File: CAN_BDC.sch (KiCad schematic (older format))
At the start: 28 parts, among them P1 CONN_01X02, P2 CONN_01X05, P3 CONN_01X02, P4 CONN_01X02, P5 CONN_01X02, P6 CONN_01X02, P7 CONN_01X04, U1 PSD2CAN, U2 SN65HVD232D, U3 POLOLU_A4988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

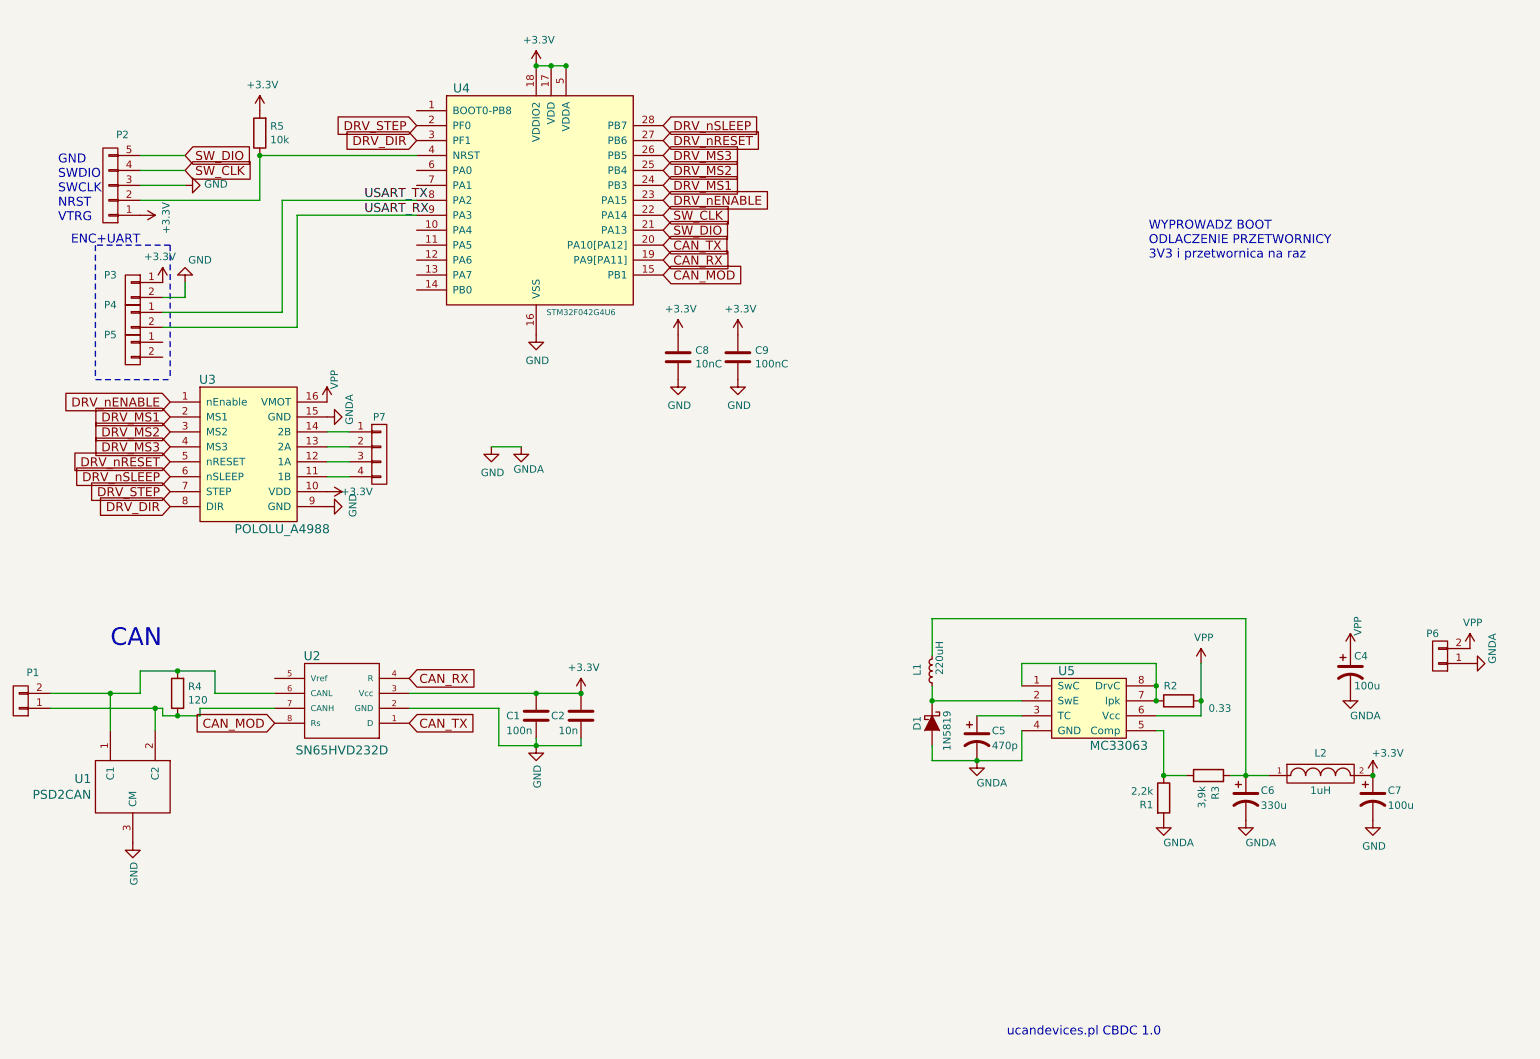
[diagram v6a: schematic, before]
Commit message: Bootconnector addition
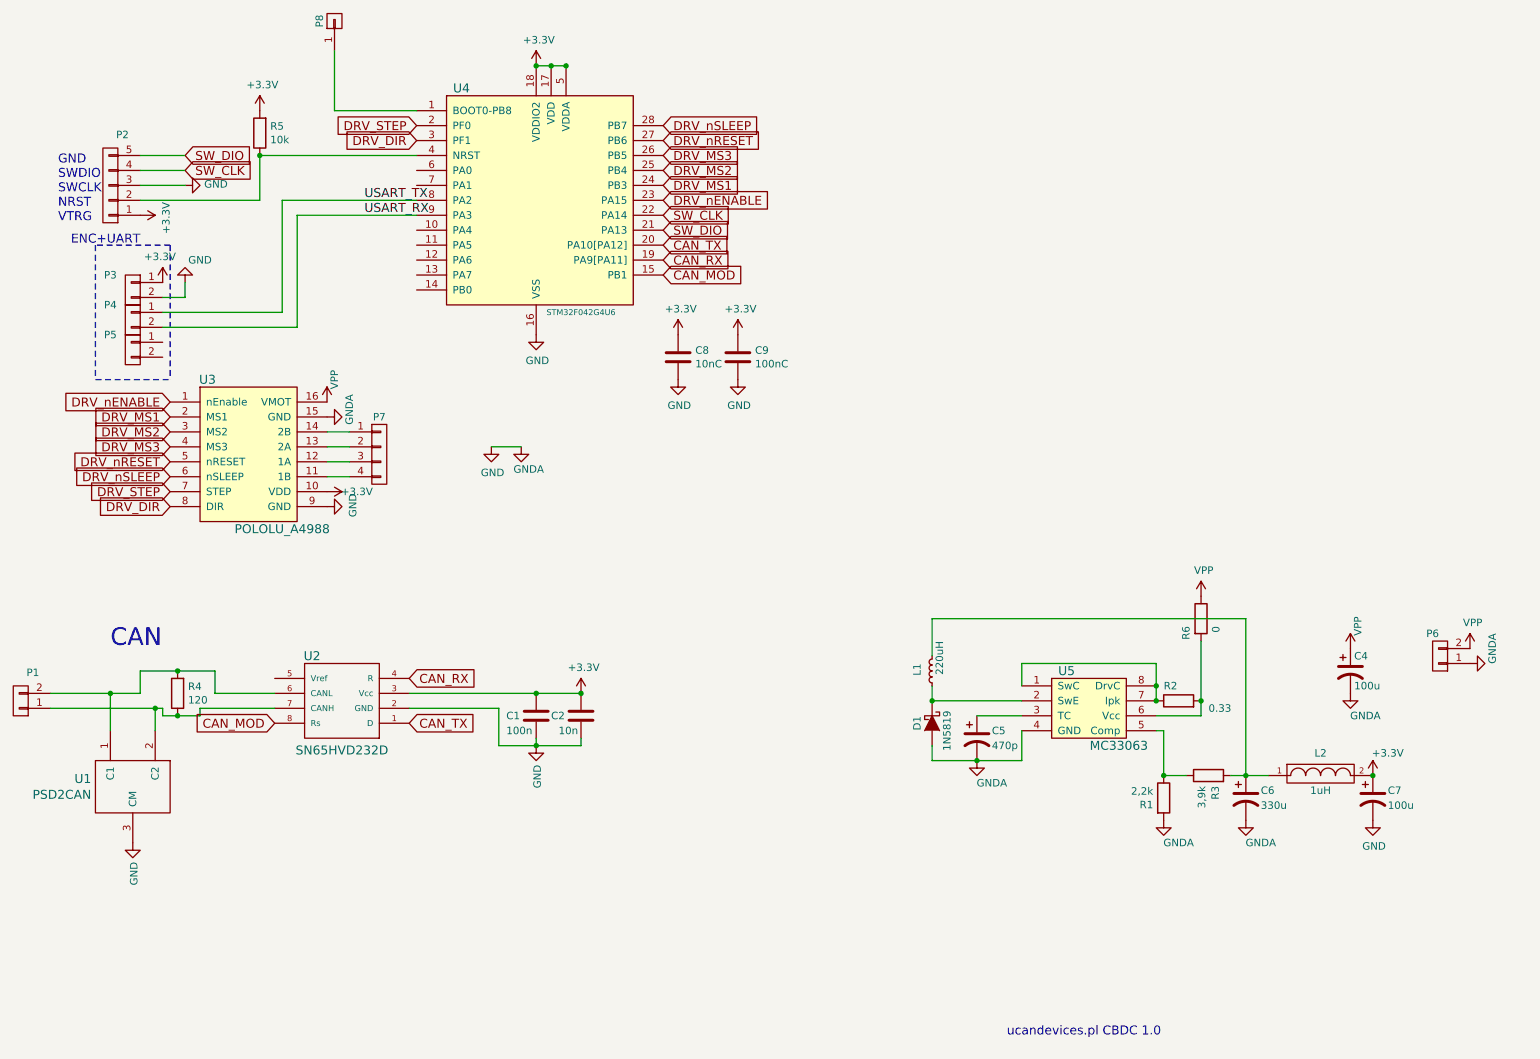
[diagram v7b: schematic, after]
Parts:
- added P8: CONN_01X01, usb_ccb_custom:smd1Conn, symbol CONN_01X01
- added R6: 0, Resistors_SMD:R_0603, symbol R
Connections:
- net VPP: now also R6.1; no longer R2.2, U5.6 (Vcc)
- net at U4.1 (BOOT0-PB8): now also P8.1 (P1)
- new net: R2.2, R6.2, U5.6 (Vcc)
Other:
- note removed: "WYPROWADZ BOOT\nODLACZENIE PRZETWORNICY\n3V3 i przetwornica na raz\n"
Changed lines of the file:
@@
 $EndDescr
 $Comp
-L GND #PWR01
+L GND #PWR14
 U 1 1 570561B2
 P 4250 2800
-F 0 "#PWR01" H 4250 2550 50  0001 C CNN
+F 0 "#PWR14" H 4250 2550 50  0001 C CNN
 F 1 "GND" H 4258 2627 50  0000 C CNN
 F 2 "" H 4250 2800 50  0000 C CNN
@@
 GND\nSWDIO\nSWCLK\nNRST\nVTRG
 $Comp
-L +3.3V #PWR02
+L +3.3V #PWR6
 U 1 1 5706E500
 P 2400 1300
-F 0 "#PWR02" H 2400 1150 50  0001 C CNN
+F 0 "#PWR6" H 2400 1150 50  0001 C CNN
 F 1 "+3.3V" H 2418 1473 50  0000 C CNN
 F 2 "" H 2400 1300 50  0000 C CNN
@@
 $EndComp
 $Comp
-L +3.3V #PWR03
+L +3.3V #PWR13
 U 1 1 5706E57B
 P 4250 1000
-F 0 "#PWR03" H 4250 850 50  0001 C CNN
+F 0 "#PWR13" H 4250 850 50  0001 C CNN
 F 1 "+3.3V" H 4268 1173 50  0000 C CNN
 F 2 "" H 4250 1000 50  0000 C CNN
@@
 $EndComp
 $Comp
-L GND #PWR04
+L GND #PWR18
 U 1 1 5706EDB2
 P 5200 3100
-F 0 "#PWR04" H 5200 2850 50  0001 C CNN
+F 0 "#PWR18" H 5200 2850 50  0001 C CNN
 F 1 "GND" H 5208 2927 50  0000 C CNN
 F 2 "" H 5200 3100 50  0000 C CNN
@@
 $EndComp
 $Comp
-L GND #PWR05
+L GND #PWR20
 U 1 1 5706EDDA
 P 5600 3100
-F 0 "#PWR05" H 5600 2850 50  0001 C CNN
+F 0 "#PWR20" H 5600 2850 50  0001 C CNN
 F 1 "GND" H 5608 2927 50  0000 C CNN
 F 2 "" H 5600 3100 50  0000 C CNN
@@
 $EndComp
 $Comp
-L +3.3V #PWR06
+L +3.3V #PWR19
 U 1 1 5706EE52
 P 5600 2800
-F 0 "#PWR06" H 5600 2650 50  0001 C CNN
+F 0 "#PWR19" H 5600 2650 50  0001 C CNN
 F 1 "+3.3V" H 5618 2973 50  0000 C CNN
 F 2 "" H 5600 2800 50  0000 C CNN
@@
 $EndComp
 $Comp
-L +3.3V #PWR07
+L +3.3V #PWR17
 U 1 1 5706EEDE
 P 5200 2800
-F 0 "#PWR07" H 5200 2650 50  0001 C CNN
+F 0 "#PWR17" H 5200 2650 50  0001 C CNN
 F 1 "+3.3V" H 5218 2973 50  0000 C CNN
 F 2 "" H 5200 2800 50  0000 C CNN
@@
 $EndComp
 $Comp
-L +3.3V #PWR08
+L +3.3V #PWR16
 U 1 1 5708A6C5
 P 4550 5200
-F 0 "#PWR08" H 4550 5050 50  0001 C CNN
+F 0 "#PWR16" H 4550 5050 50  0001 C CNN
 F 1 "+3.3V" H 4568 5373 50  0000 C CNN
 F 2 "" H 4550 5200 50  0000 C CNN
@@
 $EndComp
 $Comp
-L GND #PWR09
+L GND #PWR15
 U 1 1 5708A9FB
 P 4250 5550
-F 0 "#PWR09" H 4250 5300 50  0001 C CNN
+F 0 "#PWR15" H 4250 5300 50  0001 C CNN
 F 1 "GND" V 4258 5422 50  0000 R CNN
 F 2 "" H 4250 5550 50  0000 C CNN
@@
 $EndComp
 $Comp
-L GND #PWR010
+L GND #PWR1
 U 1 1 5708D67B
 P 1550 6200
-F 0 "#PWR010" H 1550 5950 50  0001 C CNN
+F 0 "#PWR1" H 1550 5950 50  0001 C CNN
 F 1 "GND" V 1558 6072 50  0000 R CNN
 F 2 "" H 1550 6200 50  0000 C CNN
@@
 SW_DIO
 $Comp
-L GND #PWR011
+L GND #PWR5
 U 1 1 571ACD79
 P 1900 2450
-F 0 "#PWR011" H 1900 2200 50  0001 C CNN
+F 0 "#PWR5" H 1900 2200 50  0001 C CNN
 F 1 "GND" H 2000 2300 50  0000 C CNN
 F 2 "" H 1900 2450 50  0000 C CNN
@@
 $EndComp
 $Comp
-L +3.3V #PWR012
+L +3.3V #PWR2
 U 1 1 57800AA2
 P 1600 2000
-F 0 "#PWR012" H 1600 1850 50  0001 C CNN
+F 0 "#PWR2" H 1600 1850 50  0001 C CNN
 F 1 "+3.3V" H 1618 2173 50  0000 C CNN
 F 2 "" H 1600 2000 50  0000 C CNN
@@
 ucandevices.pl CBDC 1.0\n
 $Comp
-L +3.3V #PWR013
+L +3.3V #PWR3
 U 1 1 57F6DF04
 P 1750 2450
-F 0 "#PWR013" H 1750 2300 50  0001 C CNN
+F 0 "#PWR3" H 1750 2300 50  0001 C CNN
 F 1 "+3.3V" H 1768 2623 50  0000 C CNN
 F 2 "" H 1750 2450 50  0000 C CNN
@@
 $EndComp
 $Comp
-L +3.3V #PWR014
+L +3.3V #PWR27
 U 1 1 57F96BE3
 P 9850 5750
-F 0 "#PWR014" H 9850 5600 50  0001 C CNN
+F 0 "#PWR27" H 9850 5600 50  0001 C CNN
 F 1 "+3.3V" H 9950 5900 50  0000 C CNN
 F 2 "" H 9850 5750 50  0000 C CNN
@@
 $EndComp
 $Comp
-L GND #PWR015
+L GND #PWR4
 U 1 1 57056C83
 P 1900 1800
-F 0 "#PWR015" H 1900 1550 50  0001 C CNN
+F 0 "#PWR4" H 1900 1550 50  0001 C CNN
 F 1 "GND" V 1908 1672 50  0000 R CNN
 F 2 "" H 1900 1800 50  0000 C CNN
@@
 $EndComp
 $Comp
-L VPP #PWR016
+L VPP #PWR29
 U 1 1 5802A676
 P 10500 4900
-F 0 "#PWR016" H 10500 4750 50  0001 C CNN
+F 0 "#PWR29" H 10500 4750 50  0001 C CNN
 F 1 "VPP" H 10518 5073 50  0000 C CNN
 F 2 "" H 10500 4900 50  0000 C CNN
@@
 ENC+UART
 $Comp
-L GNDA #PWR017
+L GNDA #PWR30
 U 1 1 5805AC7E
 P 10500 5000
-F 0 "#PWR017" H 10500 4750 50  0001 C CNN
+F 0 "#PWR30" H 10500 4750 50  0001 C CNN
 F 1 "GNDA" H 10600 4850 50  0000 C CNN
 F 2 "" H 10500 5000 50  0000 C CNN
@@
 $EndComp
 $Comp
-L VPP #PWR018
+L VPP #PWR7
 U 1 1 5808D6A9
 P 2850 3250
-F 0 "#PWR018" H 2850 3100 50  0001 C CNN
+F 0 "#PWR7" H 2850 3100 50  0001 C CNN
 F 1 "VPP" V 2900 3400 50  0000 C CNN
 F 2 "" H 2850 3250 50  0000 C CNN
@@
 $EndComp
 $Comp
-L GNDA #PWR019
+L GNDA #PWR8
 U 1 1 5808DF8A
 P 2850 3350
-F 0 "#PWR019" H 2850 3100 50  0001 C CNN
+F 0 "#PWR8" H 2850 3100 50  0001 C CNN
 F 1 "GNDA" H 2900 3200 50  0000 C CNN
 F 2 "" H 2850 3350 50  0000 C CNN
@@
 DRV_MS3
 $Comp
-L +3.3V #PWR020
+L +3.3V #PWR9
 U 1 1 5809060D
 P 2850 3850
-F 0 "#PWR020" H 2850 3700 50  0001 C CNN
+F 0 "#PWR9" H 2850 3700 50  0001 C CNN
 F 1 "+3.3V" V 2850 4050 50  0000 C CNN
 F 2 "" H 2850 3850 50  0000 C CNN
@@
 $EndComp
 $Comp
-L GNDA #PWR021
+L GNDA #PWR26
 U 1 1 58095023
 P 9700 5200
-F 0 "#PWR021" H 9700 4950 50  0001 C CNN
+F 0 "#PWR26" H 9700 4950 50  0001 C CNN
 F 1 "GNDA" H 9800 5050 50  0000 C CNN
 F 2 "" H 9700 5200 50  0000 C CNN
@@
 $EndComp
 $Comp
-L VPP #PWR022
+L VPP #PWR25
 U 1 1 5809511F
 P 9700 4900
-F 0 "#PWR022" H 9700 4750 50  0001 C CNN
+F 0 "#PWR25" H 9700 4750 50  0001 C CNN
 F 1 "VPP" V 9750 5050 50  0000 C CNN
 F 2 "" H 9700 4900 50  0000 C CNN
@@
 Connection ~ 8400 5150
 $Comp
-L VPP #PWR023
+L VPP #PWR23
 U 1 1 580A2B8E
-P 8700 5000
-F 0 "#PWR023" H 8700 4850 50  0001 C CNN
-F 1 "VPP" H 8718 5173 50  0000 C CNN
-F 2 "" H 8700 5000 50  0000 C CNN
-F 3 "" H 8700 5000 50  0000 C CNN
-	1    8700 5000
-	1    0    0    -1
-$EndComp
-Wire Wire Line
-	8700 5000 8700 5350
+P 8700 4550
+F 0 "#PWR23" H 8700 4400 50  0001 C CNN
+F 1 "VPP" H 8718 4723 50  0000 C CNN
+F 2 "" H 8700 4550 50  0000 C CNN
+F 3 "" H 8700 4550 50  0000 C CNN
+	1    8700 4550
+	1    0    0    -1
+$EndComp
+Wire Wire Line
+	8700 4850 8700 5350
 Connection ~ 8700 5250
 Wire Wire Line
@@
 	8900 5750 9150 5750
 $Comp
-L GNDA #PWR024
+L GNDA #PWR21
 U 1 1 580A3786
 P 7200 5650
-F 0 "#PWR024" H 7200 5400 50  0001 C CNN
+F 0 "#PWR21" H 7200 5400 50  0001 C CNN
 F 1 "GNDA" H 7300 5500 50  0000 C CNN
 F 2 "" H 7200 5650 50  0000 C CNN
@@
 $EndComp
 $Comp
-L GNDA #PWR025
+L GNDA #PWR22
 U 1 1 580A3846
 P 8450 6050
-F 0 "#PWR025" H 8450 5800 50  0001 C CNN
+F 0 "#PWR22" H 8450 5800 50  0001 C CNN
 F 1 "GNDA" H 8550 5900 50  0000 C CNN
 F 2 "" H 8450 6050 50  0000 C CNN
@@
 $EndComp
 $Comp
-L GNDA #PWR026
+L GNDA #PWR24
 U 1 1 580A3906
 P 9000 6050
-F 0 "#PWR026" H 9000 5800 50  0001 C CNN
+F 0 "#PWR24" H 9000 5800 50  0001 C CNN
 F 1 "GNDA" H 9100 5900 50  0000 C CNN
 F 2 "" H 9000 6050 50  0000 C CNN
@@
 Connection ~ 9850 5750
 $Comp
-L GND #PWR027
+L GND #PWR28
 U 1 1 580A4A8C
 P 9850 6050
-F 0 "#PWR027" H 9850 5800 50  0001 C CNN
+F 0 "#PWR28" H 9850 5800 50  0001 C CNN
 F 1 "GND" H 9858 5877 50  0000 C CNN
 F 2 "" H 9850 6050 50  0000 C CNN
@@
 Connection ~ 8400 5250
 $Comp
-L GND #PWR028
+L GND #PWR10
 U 1 1 580A6796
 P 2850 3950
-F 0 "#PWR028" H 2850 3700 50  0001 C CNN
+F 0 "#PWR10" H 2850 3700 50  0001 C CNN
 F 1 "GND" H 2858 3777 50  0000 C CNN
 F 2 "" H 2850 3950 50  0000 C CNN
@@
 $EndComp
 $Comp
-L GNDA #PWR029
+L GNDA #PWR12
 U 1 1 580A6A98
 P 4150 3550
-F 0 "#PWR029" H 4150 3300 50  0001 C CNN
+F 0 "#PWR12" H 4150 3300 50  0001 C CNN
 F 1 "GNDA" H 4200 3400 50  0000 C CNN
 F 2 "" H 4150 3550 50  0000 C CNN
@@
 $EndComp
 $Comp
-L GND #PWR030
+L GND #PWR11
 U 1 1 580A6AF4
 P 3950 3550
-F 0 "#PWR030" H 3950 3300 50  0001 C CNN
+F 0 "#PWR11" H 3950 3300 50  0001 C CNN
 F 1 "GND" H 3958 3377 50  0000 C CNN
 F 2 "" H 3950 3550 50  0000 C CNN
@@
 	2100 5200 2500 5200
 Connection ~ 1850 5050
-Text Notes 8350 2300 0    60   ~ 0
-WYPROWADZ BOOT\nODLACZENIE PRZETWORNICY\n3V3 i przetwornica na raz\n
 Text Label 3100 2000 0    60   ~ 0
 USART_RX
@@
 Wire Wire Line
 	2550 2650 1750 2650
+$Comp
+L R R6
+U 1 1 580F5FDB
+P 8700 4700
+F 0 "R6" V 8600 4650 50  0000 R CNN
+F 1 "0" V 8800 4650 50  0000 R CNN
+F 2 "Resistors_SMD:R_0603" H 8630 4791 50  0001 R CNN
+F 3 "" H 8700 4700 50  0000 C CNN
+	1    8700 4700
+	1    0    0    -1
+$EndComp
+Wire Wire Line
+	3450 1300 2900 1300
+Wire Wire Line
+	2900 1300 2900 900
+$Comp
+L CONN_01X01 P8
+U 1 1 580FE1FB
+P 2900 700
+F 0 "P8" H 2900 800 50  0000 C CNN
+F 1 "CONN_01X01" V 3000 700 50  0001 C CNN
+F 2 "usb_ccb_custom:smd1Conn" H 2900 700 50  0001 C CNN
+F 3 "" H 2900 700 50  0000 C CNN
+	1    2900 700
+	0    -1   -1   0
+$EndComp
 $EndSCHEMATC

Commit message: Fids addition
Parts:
- added P9: CONN_01X02, Pin_Headers:Pin_Header_Straight_1x02_Pitch2.00mm, symbol CONN_01X02
- added f1, f2: fiducial, Fiducials:Fiducial_1mm_Dia_2.54mm_Outer_CopperTop, symbol fiducial
- added f3, f4: fiducial, Fiducials:Fiducial_1mm_Dia_2.54mm_Outer_CopperBottom, symbol fiducial
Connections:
- net GPIO1: now reaches U4.10 (PA4)
- net GPIO1: now also P5.1 (P1)
- net GPIO2: now reaches U4.11 (PA5)
- net GPIO2: now also P5.2 (P2)
- net GPIO3: now reaches U4.12 (PA6)
- net GPIO3: now also P9.1 (P1)
- net GPIO4: now reaches U4.13 (PA7)
- net GPIO4: now also P9.2 (P2)
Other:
- moved on the sheet: P7, U3
